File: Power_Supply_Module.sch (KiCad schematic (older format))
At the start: 4 parts, among them Con3 USB_C_Wurth_632723130112

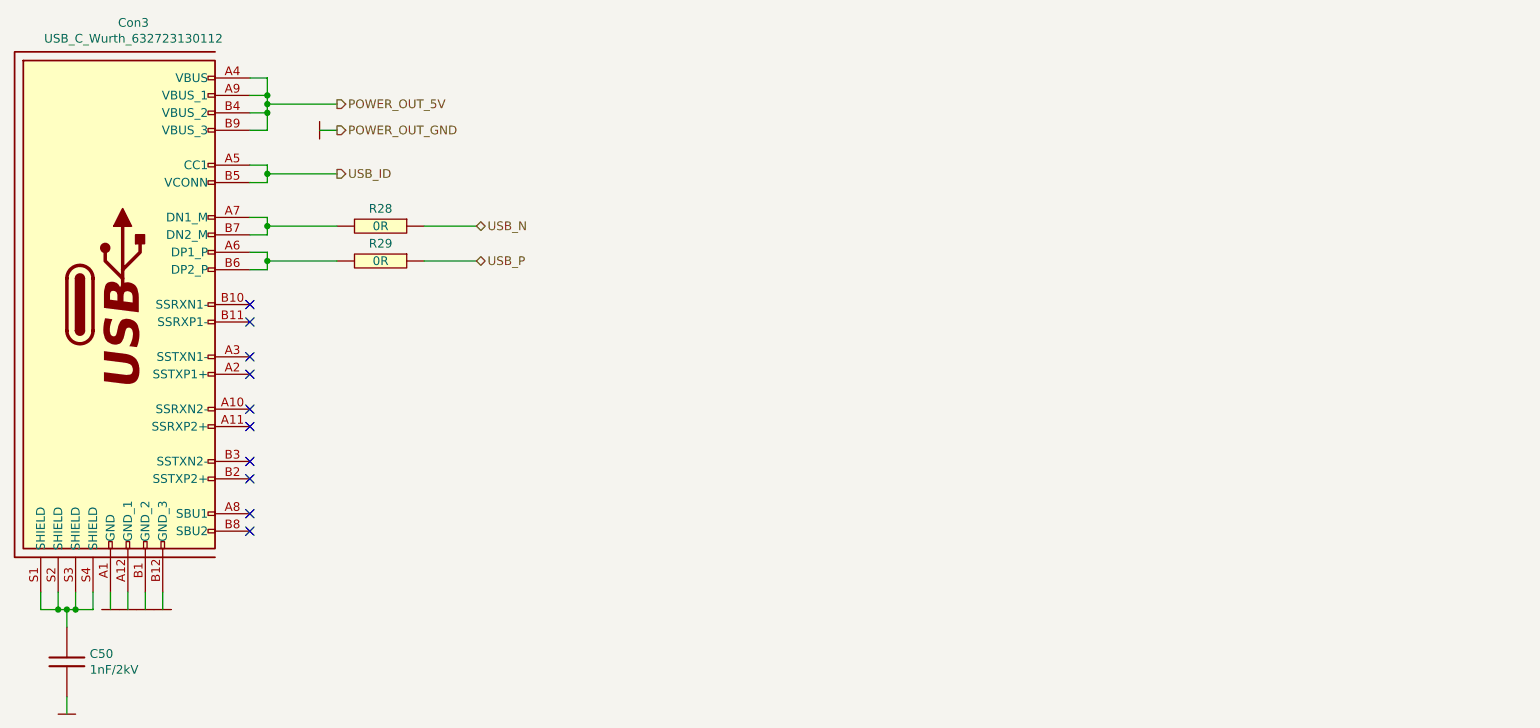
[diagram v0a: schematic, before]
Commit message: Schematic finished, with check ERC
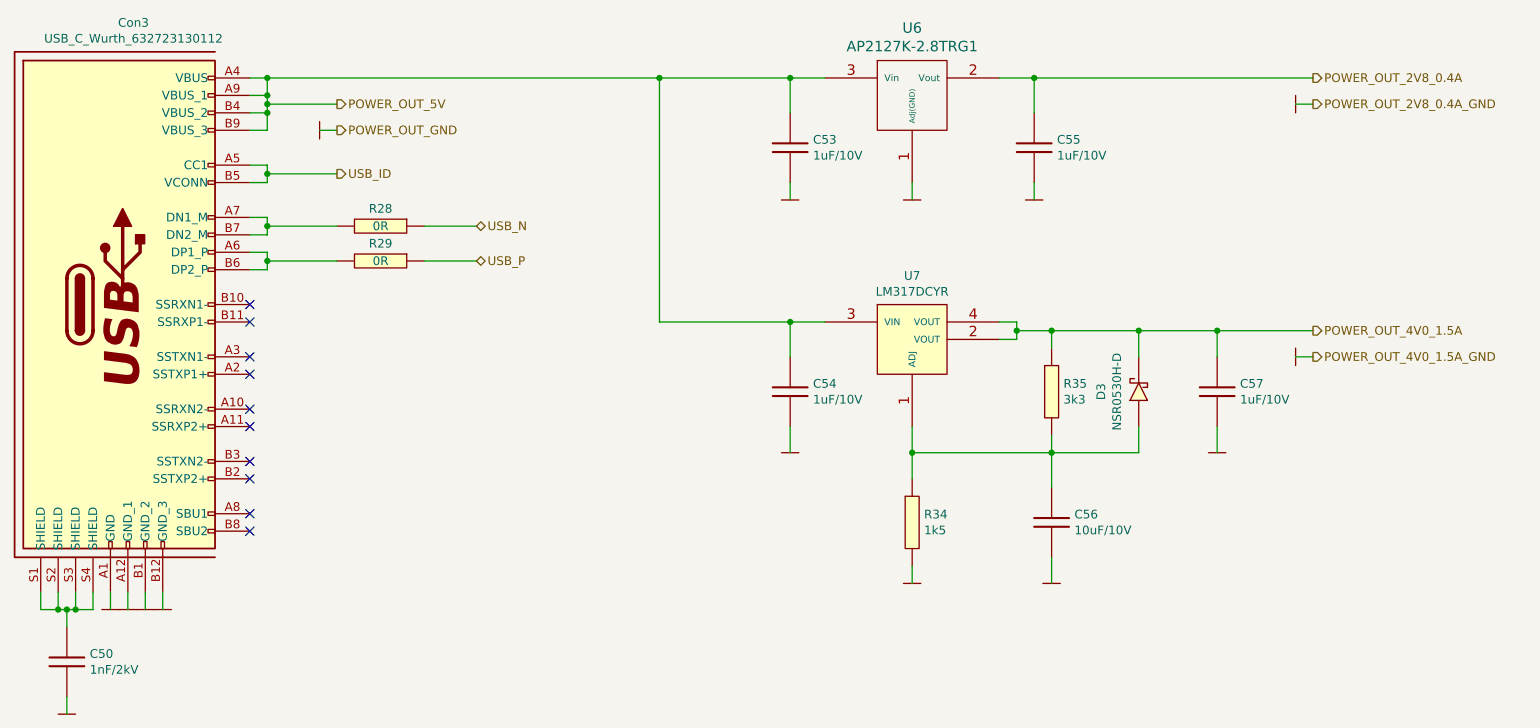
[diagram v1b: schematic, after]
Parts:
- added C53, C54, C55, C57: 1uF/10V, Capacitors_Smd_0402:1uF_0402, symbol Capacitors_Smd0402:1uF_0402
- added C56: 10uF/10V, Capacitors_Smd_0603:10uF_10V_0603, symbol Capacitors_Smd0603:10uF_0603
- added D3: NSR0530H-D, Diodes:NSR0530H-D_SOD323, symbol Diodes:NSR0530H-D
- added R34: 1k5, Resistor_Smd_0402:1k5_0402, symbol Resistors_Smd0402:1k5_0402
- added R35: 3k3, Resistor_Smd_0402:3k3_0402, symbol Resistors_Smd0402:3k3_0402
- added U6: AP2127K-2.8TRG1, Linear:AP2127K-2.8TRG1_SOT23, symbol Linear_Regulators:AP2127K-2.8TRG1
- added U7: LM317DCYR, Linear:LM317DCYR_SOT223, symbol Linear_Regulators:LM317DCYR
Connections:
- net GND: now also C53.2, C54.2, C55.2, C56.2, C57.2, R34.2, U6.1 (Adj(GND))
- net POWER_OUT_5V: now also C53.1, C54.1, U6.3 (Vin), U7.3 (VIN)
- new net: C56.1, D3.2 (A), R34.1, R35.2, U7.1 (ADJ)
- new net POWER_OUT_2V8_0.4A: C55.1, U6.2 (Vout)
- new net POWER_OUT_4V0_1.5A: C57.1, D3.1 (K), R35.1, U7.2 (VOUT), U7.4 (VOUT)

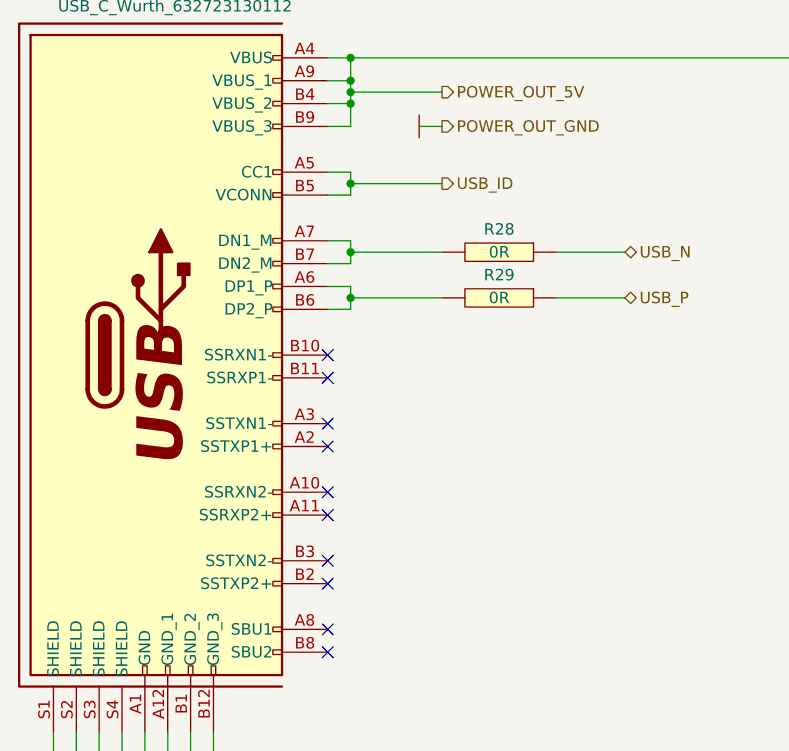
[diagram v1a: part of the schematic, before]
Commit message: Added all connections, usb and ethernet track not aligned yet, component references not aligned, gerbers not generated
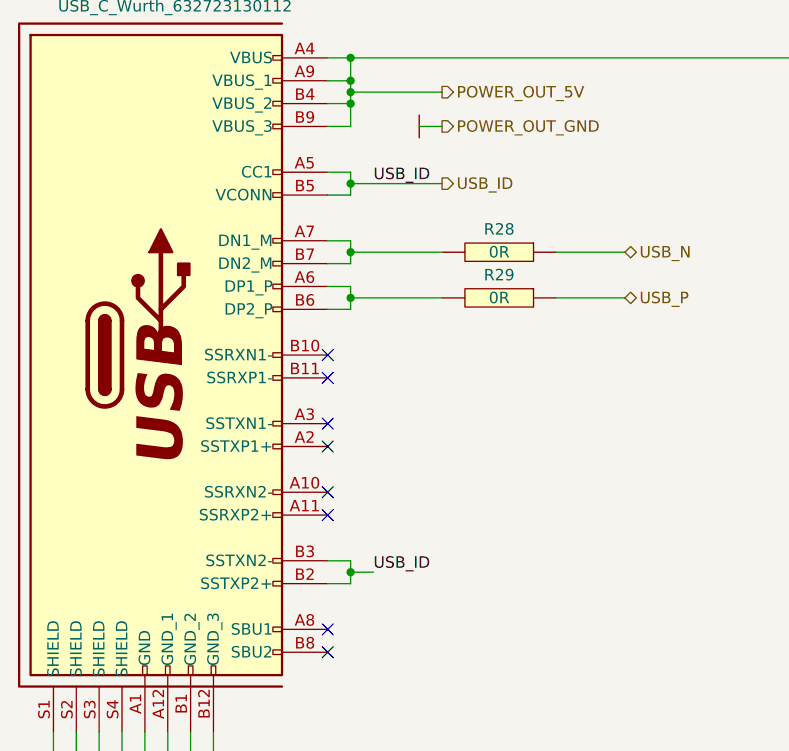
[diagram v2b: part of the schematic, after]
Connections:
- net USB_ID: now also Con3.B2 (SSTXP2+), Con3.B3 (SSTXN2-)
- no-connect marks 10 -> 8
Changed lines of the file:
@@
 NoConn ~ 5050 6550
 NoConn ~ 5050 6450
-NoConn ~ 5050 6250
-NoConn ~ 5050 6150
 NoConn ~ 5050 5950
 NoConn ~ 5050 5850
@@
 	11150 5400 10600 5400
 Connection ~ 10600 5400
+Wire Wire Line
+	5050 6150 5150 6150
+Wire Wire Line
+	5150 6150 5150 6200
+Wire Wire Line
+	5150 6250 5050 6250
+Text Label 5250 4500 0    50   ~ 0
+USB_ID
+Text Label 5250 6200 0    50   ~ 0
+USB_ID
+Wire Wire Line
+	5250 6200 5150 6200
+Connection ~ 5150 6200
+Wire Wire Line
+	5150 6200 5150 6250
 $EndSCHEMATC
